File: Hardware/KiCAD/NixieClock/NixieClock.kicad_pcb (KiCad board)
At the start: 2 copper layers, 203.2 x 61 mm, 16 parts, among them IC1 , IC2 

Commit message: Nixie power supply placed, HV lines routed
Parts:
- added REF**: , Connector_PinHeader_2.54mm:PinHeader_1x02_P2.54mm_Vertical, F.Cu at (241.9, 87.7)
- added REF**: , Connector_PinHeader_2.54mm:PinHeader_1x03_P2.54mm_Vertical, F.Cu at (266.4, 83.2)
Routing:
- net (no net): track 2986.3 -> 3179.2 mm
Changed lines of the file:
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@@
     (thickness 1.6)
     (drawings 4)
-    (tracks 409)
+    (tracks 443)
     (zones 0)
-    (modules 16)
+    (modules 18)
     (nets 1)
   )
@@
       (outputformat 1)
       (mirror false)
-      (drillshape 1)
+      (drillshape 0)
       (scaleselection 1)
       (outputdirectory ""))
@@
     (uvia_dia 0.3)
     (uvia_drill 0.1)
+  )
+  (module Connector_PinHeader_2.54mm:PinHeader_1x02_P2.54mm_Vertical (layer F.Cu)
+    (at 241.935 87.7189 180)
+    (descr "Through hole straight pin header, 1x02, 2.54mm pitch, single row")
+    (tags "Through hole pin header THT 1x02 2.54mm single row")
+    (fp_text reference REF** (at 0 -2.33) (layer F.SilkS)
+      (effects (font (size 1 1) (thickness 0.15)))
+    )
+    (fp_text value " " (at 0 4.87) (layer F.Fab)
+      (effects (font (size 1 1) (thickness 0.15)))
+    )
+    (fp_line (start -0.635 -1.27) (end 1.27 -1.27) (layer F.Fab) (width 0.1))
+    (fp_line (start 1.27 -1.27) (end 1.27 3.81) (layer F.Fab) (width 0.1))
+    (fp_line (start 1.27 3.81) (end -1.27 3.81) (layer F.Fab) (width 0.1))
+    (fp_line (start -1.27 3.81) (end -1.27 -0.635) (layer F.Fab) (width 0.1))
+    (fp_line (start -1.27 -0.635) (end -0.635 -1.27) (layer F.Fab) (width 0.1))
+    (fp_line (start -1.33 3.87) (end 1.33 3.87) (layer F.SilkS) (width 0.12))
+    (fp_line (start -1.33 1.27) (end -1.33 3.87) (layer F.SilkS) (width 0.12))
+    (fp_line (start 1.33 1.27) (end 1.33 3.87) (layer F.SilkS) (width 0.12))
+    (fp_line (start -1.33 1.27) (end 1.33 1.27) (layer F.SilkS) (width 0.12))
+    (fp_line (start -1.33 0) (end -1.33 -1.33) (layer F.SilkS) (width 0.12))
+    (fp_line (start -1.33 -1.33) (end 0 -1.33) (layer F.SilkS) (width 0.12))
+    (fp_line (start -1.8 -1.8) (end -1.8 4.35) (layer F.CrtYd) (width 0.05))
+    (fp_line (start -1.8 4.35) (end 1.8 4.35) (layer F.CrtYd) (width 0.05))
+    (fp_line (start 1.8 4.35) (end 1.8 -1.8) (layer F.CrtYd) (width 0.05))
+    (fp_line (start 1.8 -1.8) (end -1.8 -1.8) (layer F.CrtYd) (width 0.05))
+    (fp_text user %R (at 0 1.27 90) (layer F.Fab)
+      (effects (font (size 1 1) (thickness 0.15)))
+    )
+    (pad 1 thru_hole rect (at 0 0 180) (size 1.7 1.7) (drill 1) (layers *.Cu *.Mask))
+    (pad 2 thru_hole oval (at 0 2.54 180) (size 1.7 1.7) (drill 1) (layers *.Cu *.Mask))
+    (model ${KISYS3DMOD}/Connector_PinHeader_2.54mm.3dshapes/PinHeader_1x02_P2.54mm_Vertical.wrl
+      (at (xyz 0 0 0))
+      (scale (xyz 1 1 1))
+      (rotate (xyz 0 0 0))
+    )
+  )
+  (module Connector_PinHeader_2.54mm:PinHeader_1x03_P2.54mm_Vertical (layer F.Cu)
+    (at 266.3952 83.185)
+    (descr "Through hole straight pin header, 1x03, 2.54mm pitch, single row")
+    (tags "Through hole pin header THT 1x03 2.54mm single row")
+    (fp_text reference REF** (at 0 -2.33) (layer F.SilkS)
+      (effects (font (size 1 1) (thickness 0.15)))
+    )
+    (fp_text value " " (at 0 7.41) (layer F.Fab)
+      (effects (font (size 1 1) (thickness 0.15)))
+    )
+    (fp_text user %R (at 0 2.54 90) (layer F.Fab)
+      (effects (font (size 1 1) (thickness 0.15)))
+    )
+    (fp_line (start 1.8 -1.8) (end -1.8 -1.8) (layer F.CrtYd) (width 0.05))
+    (fp_line (start 1.8 6.85) (end 1.8 -1.8) (layer F.CrtYd) (width 0.05))
+    (fp_line (start -1.8 6.85) (end 1.8 6.85) (layer F.CrtYd) (width 0.05))
+    (fp_line (start -1.8 -1.8) (end -1.8 6.85) (layer F.CrtYd) (width 0.05))
+    (fp_line (start -1.33 -1.33) (end 0 -1.33) (layer F.SilkS) (width 0.12))
+    (fp_line (start -1.33 0) (end -1.33 -1.33) (layer F.SilkS) (width 0.12))
+    (fp_line (start -1.33 1.27) (end 1.33 1.27) (layer F.SilkS) (width 0.12))
+    (fp_line (start 1.33 1.27) (end 1.33 6.41) (layer F.SilkS) (width 0.12))
+    (fp_line (start -1.33 1.27) (end -1.33 6.41) (layer F.SilkS) (width 0.12))
+    (fp_line (start -1.33 6.41) (end 1.33 6.41) (layer F.SilkS) (width 0.12))
+    (fp_line (start -1.27 -0.635) (end -0.635 -1.27) (layer F.Fab) (width 0.1))
+    (fp_line (start -1.27 6.35) (end -1.27 -0.635) (layer F.Fab) (width 0.1))
+    (fp_line (start 1.27 6.35) (end -1.27 6.35) (layer F.Fab) (width 0.1))
+    (fp_line (start 1.27 -1.27) (end 1.27 6.35) (layer F.Fab) (width 0.1))
+    (fp_line (start -0.635 -1.27) (end 1.27 -1.27) (layer F.Fab) (width 0.1))
+    (pad 3 thru_hole oval (at 0 5.08) (size 1.7 1.7) (drill 1) (layers *.Cu *.Mask))
+    (pad 2 thru_hole oval (at 0 2.54) (size 1.7 1.7) (drill 1) (layers *.Cu *.Mask))
+    (pad 1 thru_hole rect (at 0 0) (size 1.7 1.7) (drill 1) (layers *.Cu *.Mask))
+    (model ${KISYS3DMOD}/Connector_PinHeader_2.54mm.3dshapes/PinHeader_1x03_P2.54mm_Vertical.wrl
+      (at (xyz 0 0 0))
+      (scale (xyz 1 1 1))
+      (rotate (xyz 0 0 0))
+    )
   )
   (module Package_DIP:DIP-16_W10.16mm locked (layer F.Cu)
@@
   (segment (start 217.116 128.27) (end 219.175 126.211) (width 0.25) (layer F.Cu) (net 0))
   (segment (start 207.91063 128.27) (end 217.116 128.27) (width 0.25) (layer F.Cu) (net 0))
-  (segment (start 251.968 102.616) (end 251.968 97.536) (width 1) (layer B.Cu) (net 0))
-  (segment (start 251.968 97.536) (end 245.364 90.932) (width 1) (layer B.Cu) (net 0))
   (segment (start 195.68 94.996) (end 191.616 90.932) (width 0.25) (layer B.Cu) (net 0))
   (segment (start 221.715 94.996) (end 217.651 90.932) (width 0.25) (layer B.Cu) (net 0))
   (segment (start 226.287 90.932) (end 226.568 90.932) (width 0.25) (layer B.Cu) (net 0))
   (segment (start 221.715 86.36) (end 226.287 90.932) (width 0.25) (layer B.Cu) (net 0))
-  (segment (start 245.364 90.932) (end 226.568 90.932) (width 1) (layer B.Cu) (net 0))
   (segment (start 195.68 86.36) (end 200.252 90.932) (width 0.25) (layer B.Cu) (net 0))
   (segment (start 147.406 127.508) (end 144.6755 127.508) (width 0.25) (layer B.Cu) (net 0))
@@
   (segment (start 177.673 111.76) (end 177.546 111.76) (width 0.25) (layer B.Cu) (net 0))
   (segment (start 177.546 111.76) (end 176.87 111.76) (width 0.25) (layer B.Cu) (net 0))
+  (segment (start 269.748 91.6178) (end 266.3952 88.265) (width 1) (layer B.Cu) (net 0))
+  (segment (start 269.748 102.616) (end 269.748 91.6178) (width 1) (layer B.Cu) (net 0))
+  (segment (start 236.8719 90.932) (end 226.568 90.932) (width 1) (layer B.Cu) (net 0))
+  (segment (start 240.085 87.7189) (end 236.8719 90.932) (width 1) (layer B.Cu) (net 0))
+  (segment (start 241.935 87.7189) (end 240.085 87.7189) (width 1) (layer B.Cu) (net 0))
+  (segment (start 266.3952 88.265) (end 266.319 88.265) (width 1) (layer B.Cu) (net 0))
+  (segment (start 265.7729 87.7189) (end 241.935 87.7189) (width 1) (layer B.Cu) (net 0))
+  (segment (start 266.319 88.265) (end 265.7729 87.7189) (width 1) (layer B.Cu) (net 0))
+  (segment (start 165.921 81.534) (end 163.635 83.82) (width 0.25) (layer B.Cu) (net 0))
+  (segment (start 162.785001 82.970001) (end 162.726001 82.970001) (width 0.25) (layer B.Cu) (net 0))
+  (segment (start 163.635 83.82) (end 162.785001 82.970001) (width 0.25) (layer B.Cu) (net 0))
+  (segment (start 161.383 81.627) (end 139.793 81.627) (width 0.25) (layer B.Cu) (net 0))
+  (segment (start 162.726001 82.970001) (end 161.383 81.627) (width 0.25) (layer B.Cu) (net 0))
+  (segment (start 139.793 81.627) (end 137.6 83.82) (width 0.25) (layer B.Cu) (net 0))
+  (segment (start 137.6 83.82) (end 137.541 83.82) (width 0.25) (layer B.Cu) (net 0))
+  (segment (start 137.541 83.82) (end 135.382 81.661) (width 0.25) (layer B.Cu) (net 0))
+  (segment (start 112.794 81.661) (end 110.635 83.82) (width 0.25) (layer B.Cu) (net 0))
+  (segment (start 114.046 81.661) (end 112.794 81.661) (width 0.25) (layer B.Cu) (net 0))
+  (segment (start 114.046 81.661) (end 113.919 81.661) (width 0.25) (layer B.Cu) (net 0))
+  (segment (start 135.382 81.661) (end 114.046 81.661) (width 0.25) (layer B.Cu) (net 0))
+  (segment (start 86.759 81.661) (end 84.6 83.82) (width 0.25) (layer B.Cu) (net 0))
+  (segment (start 110.635 83.82) (end 108.476 81.661) (width 0.25) (layer B.Cu) (net 0))
+  (segment (start 108.476 81.661) (end 86.759 81.661) (width 0.25) (layer B.Cu) (net 0))
+  (segment (start 215.785001 82.970001) (end 215.785001 82.943001) (width 0.25) (layer B.Cu) (net 0))
+  (segment (start 216.635 83.82) (end 215.785001 82.970001) (width 0.25) (layer B.Cu) (net 0))
+  (segment (start 215.785001 82.943001) (end 214.503 81.661) (width 0.25) (layer B.Cu) (net 0))
+  (segment (start 192.759 81.661) (end 190.6 83.82) (width 0.25) (layer B.Cu) (net 0))
+  (segment (start 214.503 81.661) (end 192.759 81.661) (width 0.25) (layer B.Cu) (net 0))
+  (segment (start 190.6 83.82) (end 189.738 82.958) (width 0.25) (layer B.Cu) (net 0))
+  (segment (start 189.738 82.958) (end 189.738 82.931) (width 0.25) (layer B.Cu) (net 0))
+  (segment (start 188.341 81.534) (end 165.921 81.534) (width 0.25) (layer B.Cu) (net 0))
+  (segment (start 189.738 82.931) (end 188.341 81.534) (width 0.25) (layer B.Cu) (net 0))
+  (segment (start 238.2901 81.534) (end 241.935 85.1789) (width 0.25) (layer B.Cu) (net 0))
+  (segment (start 218.948 81.534) (end 238.2901 81.534) (width 0.25) (layer B.Cu) (net 0))
+  (segment (start 217.511999 82.970001) (end 218.948 81.534) (width 0.25) (layer B.Cu) (net 0))
+  (segment (start 216.635 83.82) (end 217.484999 82.970001) (width 0.25) (layer B.Cu) (net 0))
+  (segment (start 217.484999 82.970001) (end 217.511999 82.970001) (width 0.25) (layer B.Cu) (net 0))
 )

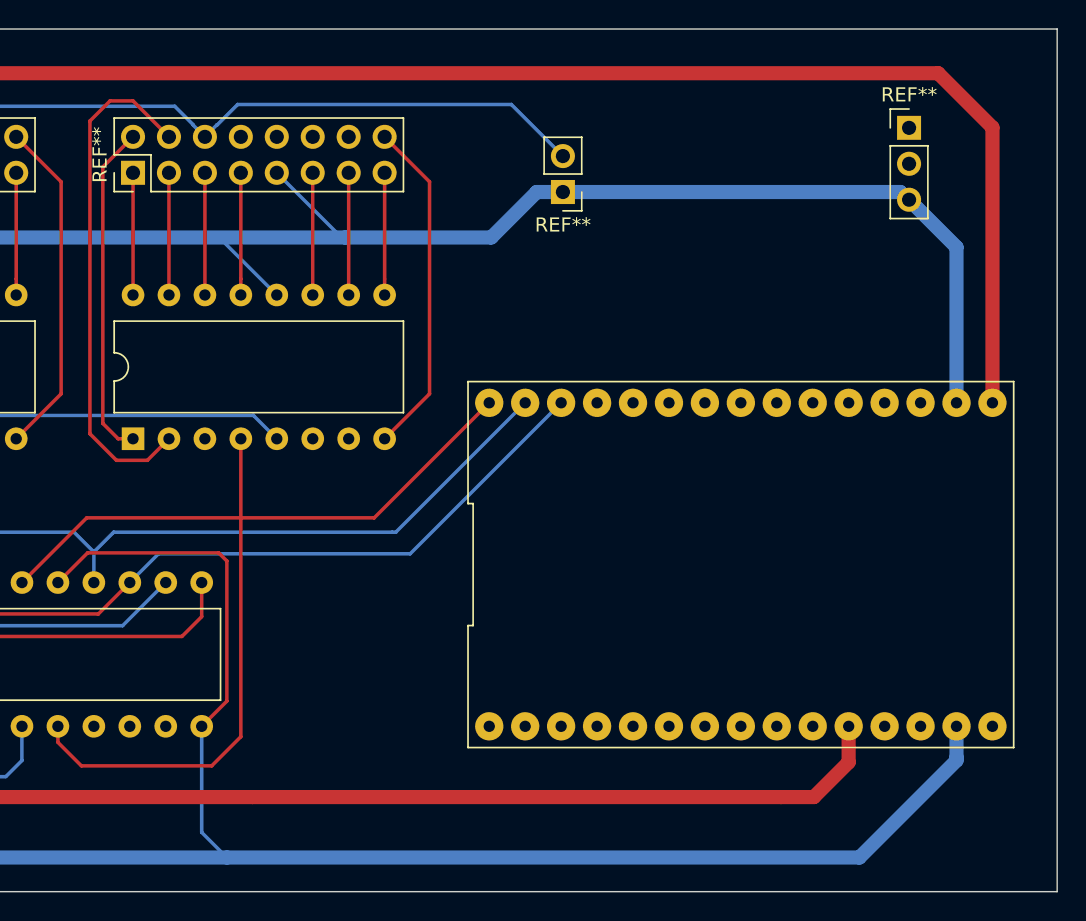
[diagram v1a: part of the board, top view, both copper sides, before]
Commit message: Placed and routed buck converter
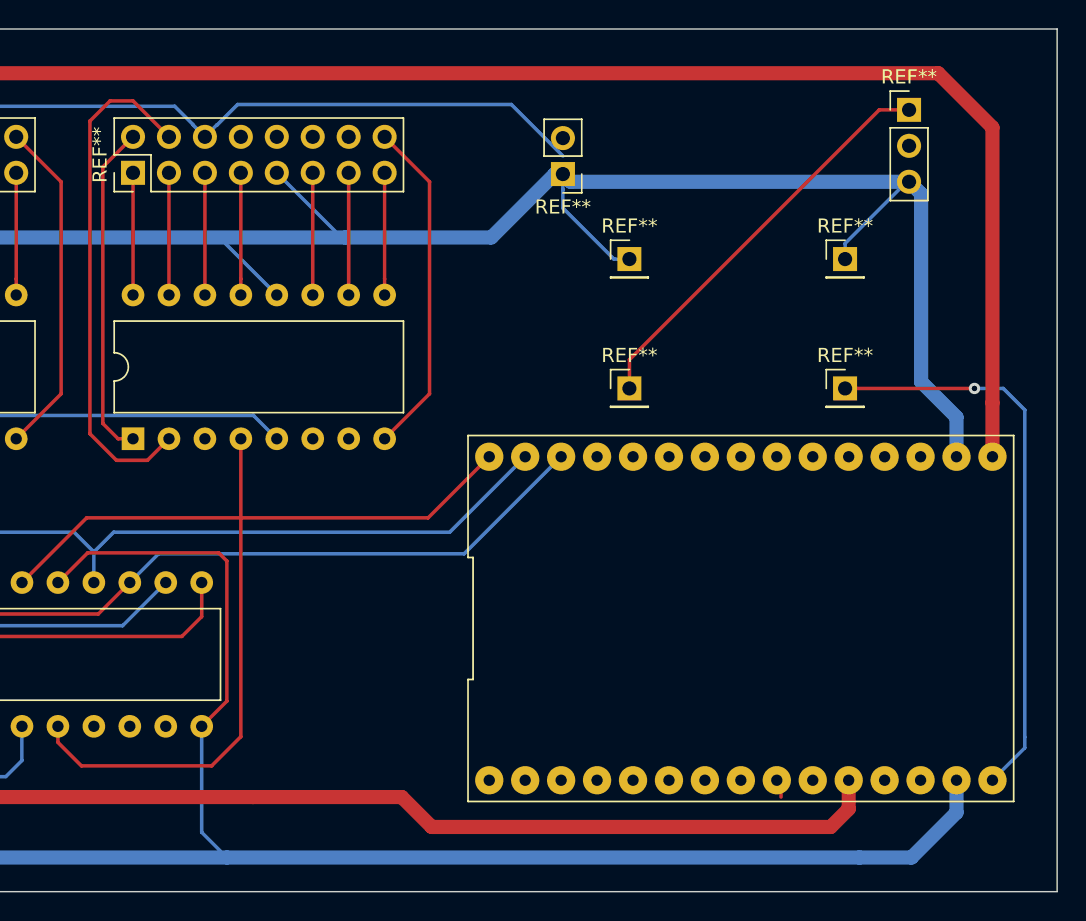
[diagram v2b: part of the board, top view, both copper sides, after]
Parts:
- added REF**: , Connector_PinHeader_2.54mm:PinHeader_1x01_P2.54mm_Vertical, F.Cu at (261.9, 101.6)
- added REF**: , Connector_PinHeader_2.54mm:PinHeader_1x01_P2.54mm_Vertical, F.Cu at (246.6, 101.6)
- added REF**: , Connector_PinHeader_2.54mm:PinHeader_1x01_P2.54mm_Vertical, F.Cu at (261.9, 92.5)
- added REF**: , Connector_PinHeader_2.54mm:PinHeader_1x01_P2.54mm_Vertical, F.Cu at (246.6, 92.5)
- moved REF** 3.81 mm to (254.5, 117.9)
- moved REF** 1.27 mm to (241.9, 86.4)
- moved REF** 1.27 mm to (266.4, 81.9)
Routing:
- net (no net): track 3179.2 -> 3267.7 mm, vias 12 -> 13

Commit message: Made power boards layouts, removed thick traces, reordered
TODO:
- Check dimmensions of power boards and node MCU
- Add mounting holes for PCB
- Add 3 push buttons and resistors
- Add diode on VIN
- Add potentiometer and ceramic resistor
- Add RGB LEDs
- Update code to match latest pin mapping
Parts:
- removed the REF** at (261.9, 101.6)
- removed the REF** at (246.6, 101.6)
- removed the REF** at (261.9, 92.5)
- removed the REF** at (246.6, 92.5)
- removed the REF** at (241.9, 86.4)
- removed the REF** at (266.4, 81.9)
- added REF**: NCH6100HV, NixieClock:NCH6100HV, F.Cu at (287.1, 104.9)
- added REF**: Mini360, NixieClock:Mini360, F.Cu at (227.2, 122.4)
- moved REF** 11.8 mm to (251.7, 106.4), turned to 270 degrees
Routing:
- net (no net): track 3267.7 -> 3294.4 mm, vias 13 -> 19
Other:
- board size 203.2 x 61 mm -> 236.2 x 61 mm

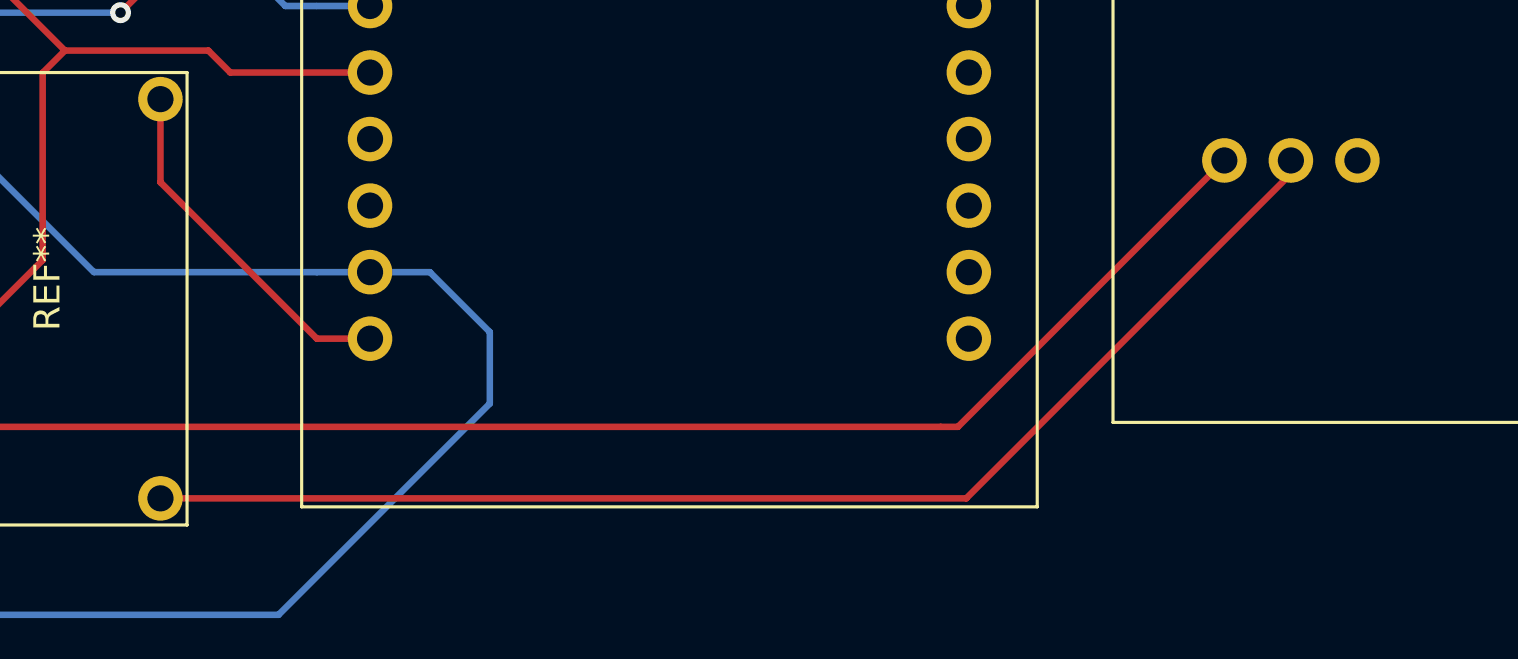
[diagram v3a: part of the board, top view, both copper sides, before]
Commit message: fixed vin pin mapping
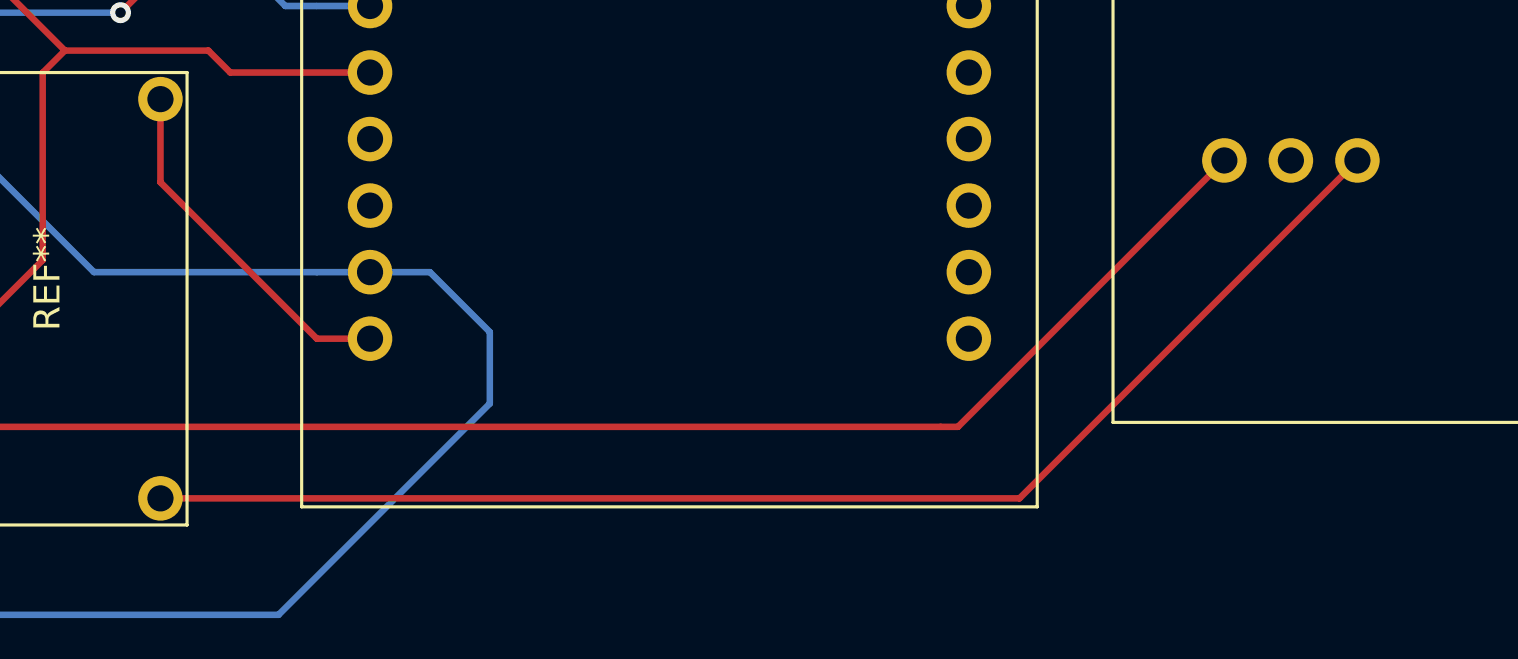
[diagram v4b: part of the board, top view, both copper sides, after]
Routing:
- net (no net): track 3294.4 -> 3296.5 mm
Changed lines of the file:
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@@
   (segment (start 232.283 115.062) (end 232.283 118.237) (width 0.25) (layer F.Cu) (net 0))
   (segment (start 225.8695 127.5715) (end 223.139 130.302) (width 0.25) (layer F.Cu) (net 0))
-  (segment (start 263.045 130.302) (end 275.945 117.402) (width 0.25) (layer F.Cu) (net 0))
-  (segment (start 232.283 130.302) (end 263.045 130.302) (width 0.25) (layer F.Cu) (net 0))
   (segment (start 237.049919 111.506) (end 233.807 108.263081) (width 0.25) (layer B.Cu) (net 0))
   (segment (start 238.252 111.506) (end 237.049919 111.506) (width 0.25) (layer B.Cu) (net 0))
@@
   (segment (start 244.856 126.6825) (end 236.7915 134.747) (width 0.25) (layer B.Cu) (net 0))
   (segment (start 111.887 134.747) (end 110.408 133.268) (width 0.25) (layer B.Cu) (net 0))
+  (segment (start 265.077 130.302) (end 277.977 117.402) (width 0.25) (layer F.Cu) (net 0))
+  (segment (start 232.283 130.302) (end 265.077 130.302) (width 0.25) (layer F.Cu) (net 0))
 )
